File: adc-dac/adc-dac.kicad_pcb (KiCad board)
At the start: 2 copper layers, 30.7 x 61.7 mm, 40 parts, among them IC12 ADS122C04IPW, J20 Conn_01x01_Pin, J24 Conn_02x01, J44 Conn_02x03_Odd_Even, SW4 SW_SPDT, U10 LM321, U22 TLV75801PDBV, U25 TCA9554ADBQR, U29 AD5593R, U7 TS5A23159DGS, U8 TS5A23159DGS

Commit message: Finished ADC/DAC board
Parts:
- removed C91, C92: 100n, Capacitor_SMD:C_0603_1608Metric
- removed C96, C97: 0.1u, Capacitor_SMD:C_0603_1608Metric
- removed J20: Conn_01x01_Pin, Connector_PinHeader_2.54mm:PinHeader_1x01_P2.54mm_Vertical
- removed J44: Conn_02x03_Odd_Even, Connector_PinSocket_2.54mm:PinSocket_2x03_P2.54mm_Vertical
- removed R85, R87, R89, R91, R93: 48.7k, Resistor_SMD:R_0603_1608Metric
- removed R86, R88, R90, R92, R94: 187k, Resistor_SMD:R_0603_1608Metric
- removed R95: 10k, Resistor_SMD:R_0603_1608Metric
- removed SW4: SW_SPDT, Button_Switch_SMD:SW_SPDT_PCM12
- removed U25: TCA9554ADBQR, Package_SO:SSOP-16_3.9x4.9mm_P0.635mm
- removed U29: AD5593R, Package_SO:TSSOP-16_4.4x5mm_P0.65mm
- added C1: 100n, Capacitor_SMD:C_0603_1608Metric, F.Cu at (94.0, 89.1)
- added C2: 100n, Capacitor_SMD:C_0603_1608Metric, F.Cu at (91.0, 96.2)
- added C3: 0.1u, Capacitor_SMD:C_0603_1608Metric, F.Cu at (95.2, 96.6)
- added G***: LOGO, heep_footprints:ESL_3x3, F.Cu at (82.3, 88.5)
- added G***: LOGO, heep_footprints:EPFL_2x7, F.Cu at (82.1, 93.8)
- added J1: Conn_02x03_Odd_Even, Connector_PinSocket_2.54mm:PinSocket_2x03_P2.54mm_Vertical, F.Cu at (109.2, 98.1)
- added J3: Conn_01x20, Connector_PinHeader_1.27mm:PinHeader_1x20_P1.27mm_Vertical, F.Cu at (84.0, 112.7)
- added J9: Conn_01x20, Connector_PinHeader_1.27mm:PinHeader_1x20_P1.27mm_Vertical, F.Cu at (79.8, 87.6)
- added R1: 10k, Resistor_SMD:R_0603_1608Metric, F.Cu at (90.6, 89.1)
- added R10: 187k, Resistor_SMD:R_0603_1608Metric, F.Cu at (100.5, 92.4)
- added R11: 48.7k, Resistor_SMD:R_0603_1608Metric, F.Cu at (102.7, 93.5)
- added R12: 187k, Resistor_SMD:R_0603_1608Metric, F.Cu at (99.5, 93.5)
- added R13: 187k, Resistor_SMD:R_0603_1608Metric, F.Cu at (97.9, 96.2)
- added R14: 187k, Resistor_SMD:R_0603_1608Metric, F.Cu at (99.4, 96.6)
- added R15: 48.7k, Resistor_SMD:R_0603_1608Metric, F.Cu at (102.8, 95.4)
- added R16: 48.7k, Resistor_SMD:R_0603_1608Metric, F.Cu at (95.6, 98.1)
- added R17: 48.7k, Resistor_SMD:R_0603_1608Metric, F.Cu at (101.6, 98.1)
- added R2: 48.7k, Resistor_SMD:R_0603_1608Metric, F.Cu at (84.7, 90.4)
- added R3: 187k, Resistor_SMD:R_0603_1608Metric, F.Cu at (87.0, 91.2)
- added R4: 48.7k, Resistor_SMD:R_0603_1608Metric, F.Cu at (84.8, 93.5)
- added R5: 48.7k, Resistor_SMD:R_0603_1608Metric, F.Cu at (84.8, 96.5)
- added R6: 187k, Resistor_SMD:R_0603_1608Metric, F.Cu at (87.0, 92.7)
- added R7: 187k, Resistor_SMD:R_0603_1608Metric, F.Cu at (87.0, 94.1)
- added R8: 187k, Resistor_SMD:R_0603_1608Metric, F.Cu at (87.2, 95.7)
- added R9: 48.7k, Resistor_SMD:R_0603_1608Metric, F.Cu at (87.2, 97.0)
- added SW1: SW_SPDT, Button_Switch_SMD:SW_SPDT_PCM12, F.Cu at (111.3, 106.2)
- added U1: AD5593R, Package_SO:TSSOP-16_4.4x5mm_P0.65mm, F.Cu at (93.2, 92.7)
- moved U3 74.8 mm to (83.3, 107.5)
- moved C4 74.1 mm to (84.0, 102.5), turned to 90 degrees
- moved R22 61.8 mm to (96.6, 108.7), turned to 90 degrees
- moved J2 61.7 mm to (99.2, 106.8), turned to 0 degrees
- moved U2 61.6 mm to (89.9, 103.2), turned to 0 degrees
- moved R24 61.0 mm to (103.5, 110.2), turned to 180 degrees
- moved R18 60.1 mm to (92.3, 99.7), turned to 180 degrees
- moved R21 59.0 mm to (107.3, 101.8), turned to -90 degrees
- moved U5 58.9 mm to (104.5, 101.8)
- moved R23 58.7 mm to (106.0, 108.0), turned to -90 degrees
- moved C8 58.6 mm to (106.4, 104.3)
- moved R20 58.6 mm to (101.6, 101.9)
- moved R19 58.4 mm to (100.1, 101.9)
- moved C7 58.3 mm to (100.8, 104.2)
- moved U6 57.8 mm to (103.1, 107.7)
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- renumbered C40 to C10, C30 to C4, C44 to C5, C43 to C6, C26 to C7, C25 to C8, C62 to C9, J24 to J2, R22 to R18, R62 to R19, R61 to R20, R11 to R21, R21 to R22, R28 to R23, R23 to R24, IC12 to U2, U8 to U3, U7 to U4, U22 to U5, U10 to U6
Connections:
- net +3.3V renamed 3V3
- net /Vpm renamed /5V
- net Net-(U10-+) renamed /ref_mid
- C10 pad 1: +3.3VA -> A3V3
- C4 pad 1: +3.3VA -> A3V3
- C7 pad 1: /3V3_ANA -> A3V3
- C9 pad 1: +3.3VA -> A3V3
- J2 pad 1: +3.3VA -> A3V3
- R20 pad 2: /3V3_ANA -> A3V3
- R24 pad 2: +3.3VA -> A3V3
- U2 pad 12: +3.3VA -> A3V3
- U3 pad 10: /ADC2 -> /ADC3
- U3 pad 2: /V_B2_o -> /ADC_2_B
- U3 pad 4: /V_B3_o -> /ADC_3_B
- U3 pad 6: /ADC3 -> /ADC2
- U3 pad 7: /V_IO_load -> /ADC_3_A
- U3 pad 8: +3.3VA -> A3V3
- U3 pad 9: /V_IO_o -> /ADC_2_A
- U4 pad 2: /V_CGRA_o -> /ADC_0_B
- U4 pad 4: /V_B1_o -> /ADC_1_B
- U4 pad 7: /V_CORE_load -> /ADC_1_A
- U4 pad 8: +3.3VA -> A3V3
- U4 pad 9: /V_CORE_o -> /ADC_0_A
- U5 pad 5: /3V3_ANA -> A3V3
- U6 pad 5: +3.3VA -> A3V3
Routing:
- net A3V3: track 0.00 -> 116.0 mm, vias 0 -> 18
- net /5V: track 1.84 -> 44.1 mm, vias 0 -> 4
- net Net-(SW1-B): track 43.3 -> 19.2 mm, vias 2 -> 0
- net /DAC7: track 0.00 -> 23.4 mm, vias 0 -> 1
- net +3.3VA: track 22.2 -> 0.00 mm, vias 1 -> 0
- net /DAC6: track 0.00 -> 22.1 mm, vias 0 -> 1
- net /DAC5: track 0.00 -> 19.7 mm, vias 0 -> 1
- net 3V3: track 19.4 -> 37.9 mm
- net /DAC4: track 0.00 -> 18.0 mm, vias 0 -> 1
- net GND: track 22.0 -> 4.51 mm, vias 0 -> 93
- net Net-(J1-Pin_3): track 2.28 -> 16.6 mm, vias 0 -> 1
- net /REF_INA: track 17.6 -> 27.7 mm, vias 0 -> 2
- net /DAC0: track 0.00 -> 10.1 mm
- net /DAC3: track 0.00 -> 10.0 mm
- net Net-(U29-IO3): track 10.0 -> 0.00 mm
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- added copper zone on B.Cu, net /5V
- added copper zone on F.Cu, net /5V
- added copper zone on F.Cu, net /ref_mid
- added copper zone on B.Cu, net A3V3
- added copper zone on F.Cu, net A3V3
- added copper zone on B.Cu, net GND
- added copper zone on F.Cu, net GND
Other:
- board size 30.7 x 61.7 mm -> 34.4 x 28.4 mm
- board text added: "3V3"
- board text added: "ADC"
- board text added: "ADC/DAC board - v1.0 - 09/25"
- board text added: "DAC"
- board text added: "GND 1V65 3V3"
- board text added: "I2C"
- board text added: "Pwr in"
- board text added: "Pwr out"
- board text added: "REF"
- board text added: "aMUXs"
- board text added: "manual sel."
- board text added: "to ADC"

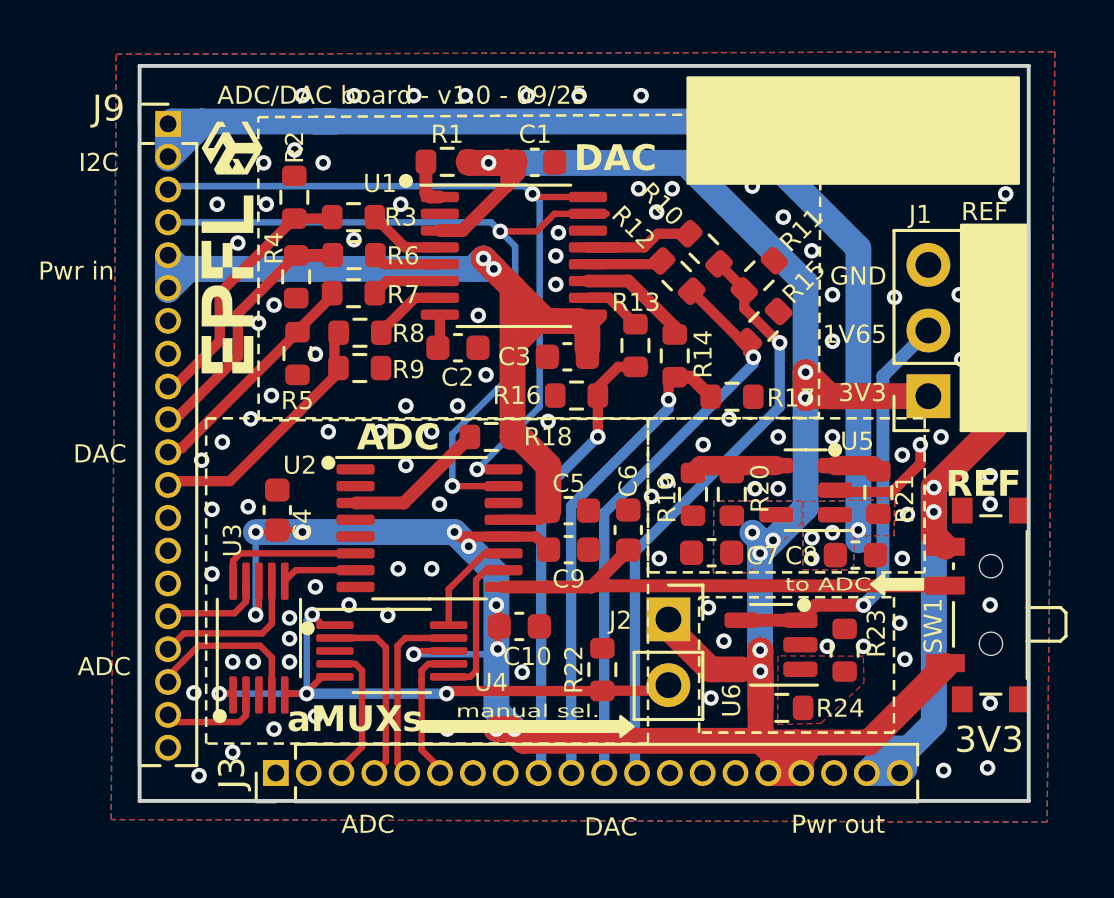
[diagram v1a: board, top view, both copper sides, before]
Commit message: re-arranged adc/dac and routed to the cgs
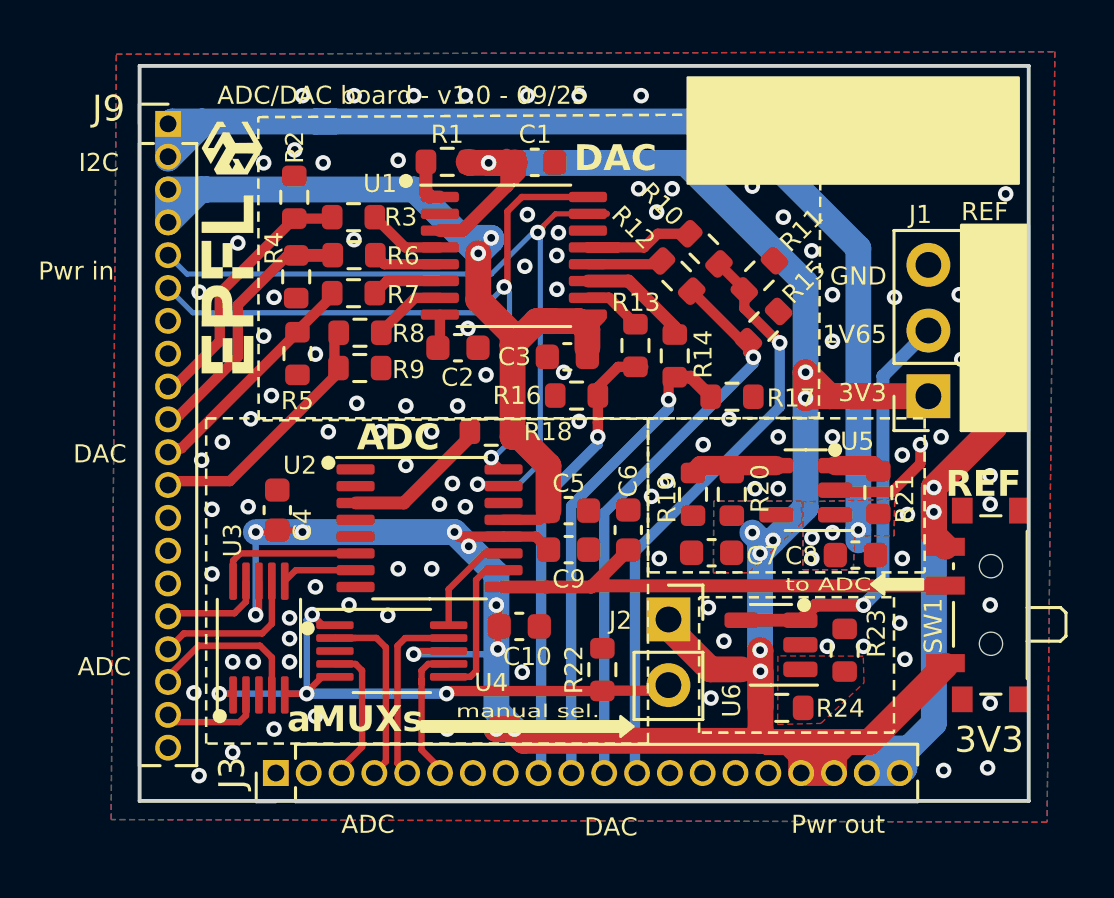
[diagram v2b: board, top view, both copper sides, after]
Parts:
- moved R18 0.20 mm to (92.3, 99.5)
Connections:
- J3 pad 16: A3V3 -> GND
- J3 pad 18: GND -> A3V3
- J9 pad 3: /SCL -> 3V3
- J9 pad 4: /SDA -> 3V3
- J9 pad 5: 3V3 -> /SDA
- J9 pad 6: 3V3 -> /SCL
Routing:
- net A3V3: track 116.0 -> 118.1 mm
- net /SCL: track 29.4 -> 27.9 mm
- net GND: vias 93 -> 98
